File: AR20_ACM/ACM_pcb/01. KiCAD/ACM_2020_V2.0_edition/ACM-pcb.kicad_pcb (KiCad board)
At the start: 2 copper layers, 19.8 x 28 mm, 32 parts, among them IC1 MCP25625T-E_ML, J1 TC2030-MCP-NL, P1 Conn_02x15_Odd_Even, Q1 Q_PMOS_DGS, U1 ATmega328P-AU, U3 NCV890430MW50TXG, Y1 16.0Mhz

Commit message: Circuit protecion fixed
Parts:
- removed D2: 2.4V, Diode_SMD:D_SOD-523
- added D4: D_Schottky_MBR0520LT1G, ACM_2020_V2:D_schotky_MBR0520LT1G, B.Cu at (74.5, 86.9)
- IC1: footprint ACM_2020_Footprintandsymbol:QFN65P600X600X100-29N-D -> ACM_2020_V2:QFN65P600X600X100-29N-D
- Q1: value Q_PMOS_DGS -> Q_PMOS_DMP3099L-13; footprint Package_TO_SOT_SMD:SOT-23 -> ACM_2020_V2:Pmos_DMP3099L-13; moved to F.Cu
- R2: value 100K Ohm -> 10K Ohm; moved to F.Cu
- moved R2 5.84 mm to (79.9, 89.4), turned to 90 degrees
- moved Q1 4.10 mm to (72.4, 88.4), turned to 90 degrees
- moved R1 1.79 mm to (69.1, 81.1), turned to 270 degrees
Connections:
- D1 pad 1: Net-(D1-Pad1) -> +12V_Safe
- F1 pad 1: Net-(D1-Pad1) -> +12V_Safe
- F1 pad 2: +12V -> Net-(D4-Pad1)
- IC1 pad 14: Net-(IC1-Pad14) -> (no net)
- IC1 pad 17: Net-(IC1-Pad17) -> (no net)
- IC1 pad 20: Net-(IC1-Pad20) -> (no net)
- IC1 pad 23: Net-(IC1-Pad23) -> (no net)
- IC1 pad 24: Net-(IC1-Pad24) -> (no net)
- IC1 pad 6: Net-(IC1-Pad6) -> (no net)
- IC1 pad 7: Net-(IC1-Pad7) -> (no net)
- IC1 pad 8: Net-(IC1-Pad8) -> (no net)
- IC1 pad 9: Net-(IC1-Pad9) -> (no net)
- J1 pad 2: +5V -> Net-(J1-Pad2)
- Q1 pad 1: Net-(D2-Pad2) -> +12V_Safe
- Q1 pad 2: +12V_Safe -> +5V
- Q1 pad 3: Net-(D1-Pad1) -> Net-(J1-Pad2)
- R2 pad 1: Net-(D2-Pad2) -> GND
- R2 pad 2: GND -> +12V_Safe
- U3 pad 2: Net-(U3-Pad2) -> (no net)
- U3 pad 6: Net-(U3-Pad6) -> (no net)
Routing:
- net +12V: track 44.4 -> 32.3 mm, vias 1 -> 0
- net Net-(D1-Pad1): track 5.04 -> 0.00 mm
- net +12V_Safe: track 13.3 -> 18.1 mm
- net Net-(D2-Pad2): track 3.50 -> 0.00 mm
- net Net-(D4-Pad1): track 0.00 -> 3.29 mm
- net Net-(J1-Pad2): track 0.00 -> 2.20 mm
- net /Reset: track 45.9 -> 43.7 mm
- net GND: track 47.1 -> 49.2 mm, vias 10 -> 11
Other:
- board text added: "V1.2"
- board text removed: "V1.1"

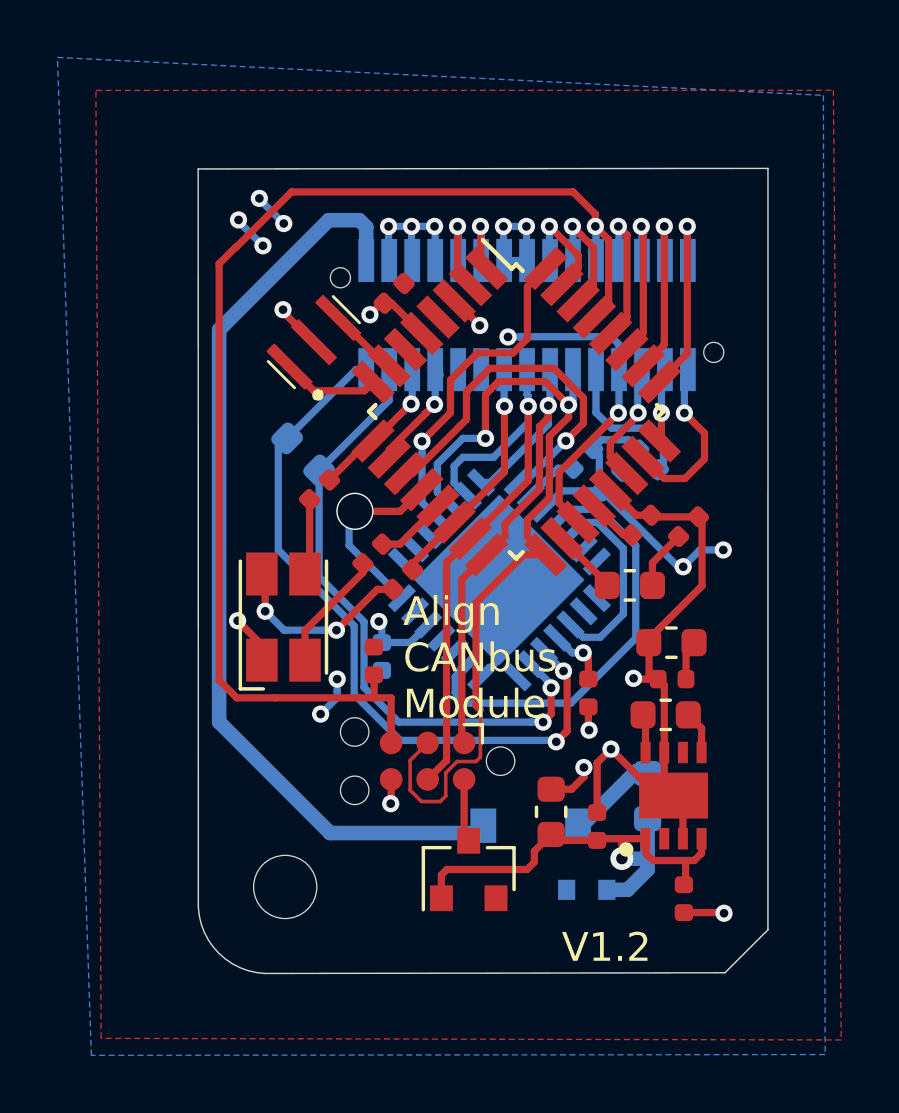
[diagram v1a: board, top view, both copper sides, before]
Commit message: Changed RGB light
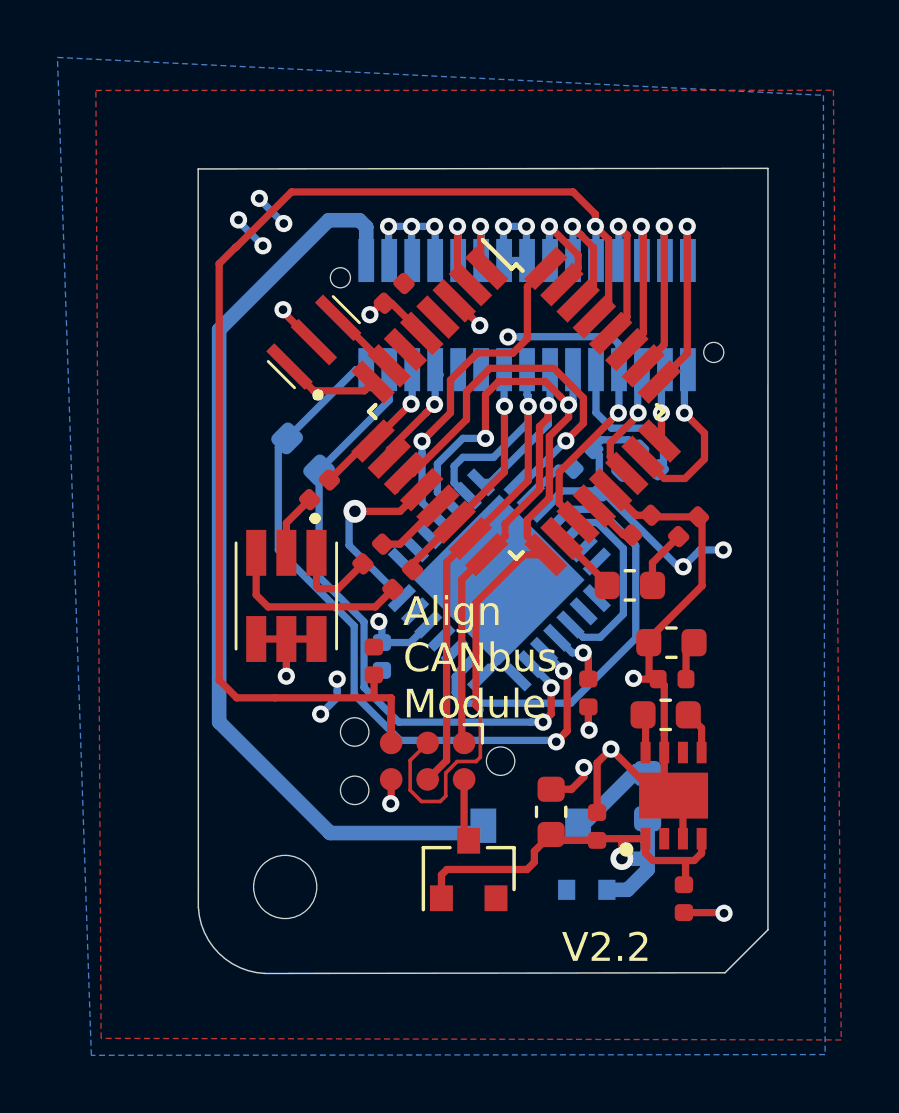
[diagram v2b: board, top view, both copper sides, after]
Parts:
- removed D3: ASMB-MTB0-0A3A2, LED_SMD:LED_Avago_PLCC4_3.2x2.8mm_CW
- added LED1: ASMB-TTF0-0A20B, ASMB-TTF0-0A20B:ASMBTTF00A20B, F.Cu at (66.0, 78.9)
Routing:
- net GND: track 49.2 -> 52.6 mm, vias 11 -> 12
- net +5V: track 32.7 -> 31.0 mm, vias 14 -> 13
- net Net-(LED1-Pad1): track 4.19 -> 3.17 mm
- net Net-(LED1-Pad5): vias 2 -> 0
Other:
- board text added: "V2.2"
- board text removed: "V1.2"

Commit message: NOT COMPLETE V3.0 ACM
This is the beginning of the V3.0 ACM. With added CAN FD transiver and CAN FD controller. 
To fix: 
Chagne CAN FD transciver to a SOCI version 
Place all capacitors in a good location. 
Board cleanup
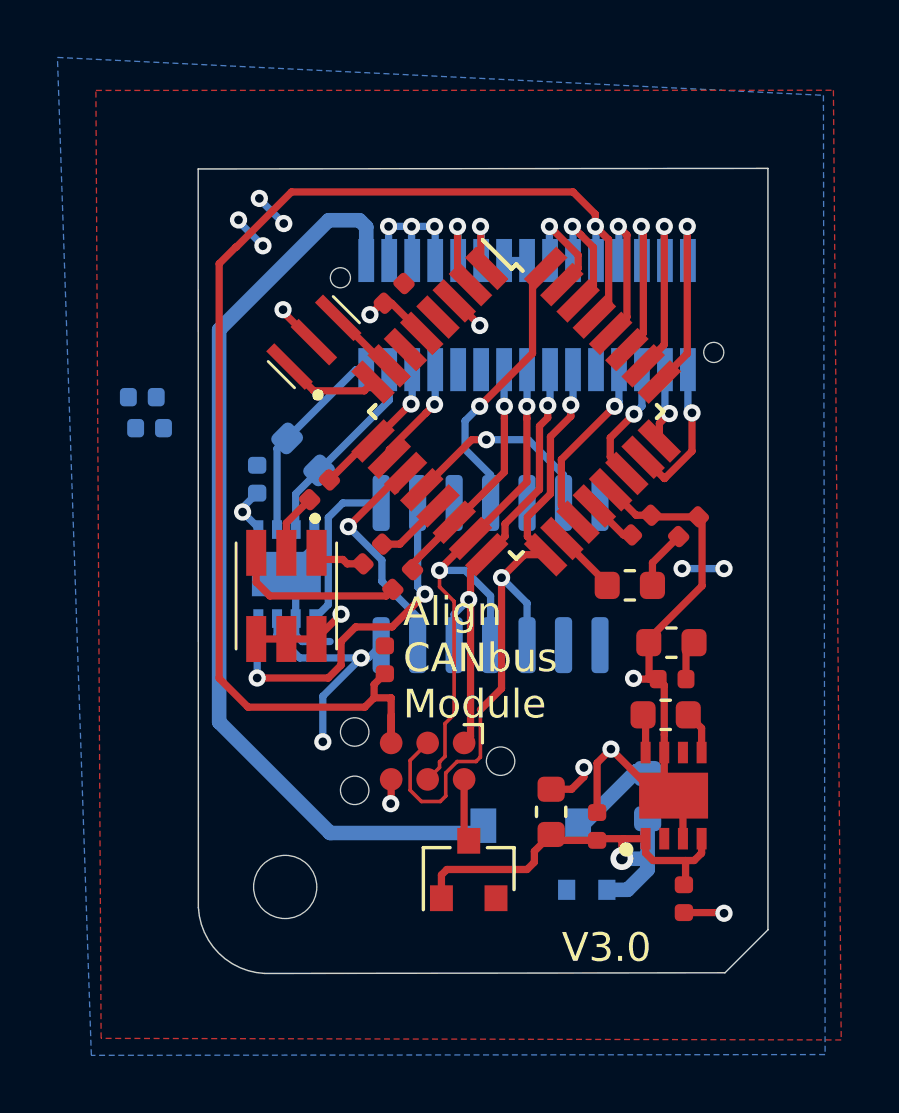
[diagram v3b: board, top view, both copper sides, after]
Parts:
- removed C9: 0.1uF, Capacitor_SMD:C_0402_1005Metric
- removed IC1: MCP25625T-E_ML, ACM_2020_V2:QFN65P600X600X100-29N-D
- removed R6: 10K Ohm, Resistor_SMD:R_0402_1005Metric
- added U2: MCP2542WFDxMF, Package_DFN_QFN:DFN-8-1EP_3x3mm_P0.65mm_EP1.55x2.4mm, B.Cu at (66.0, 78.1)
- added U4: MCP2517FD-xSL, ACM_2020_V2:Can_MCP2517FD_SOIC, B.Cu at (73.2, 78.1)
- R3: value 290 ohm -> R-Device-ACM_Y2020V0.1-rescue
- moved C6 17.4 mm to (61.3, 73.0), turned to 0 degrees
- moved C7 12.4 mm to (65.0, 74.8), turned to 90 degrees
- moved C8 12.3 mm to (61.0, 71.9), turned to 180 degrees
- moved R1 0.38 mm to (69.5, 81.1)
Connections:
- C8 pad 1: +5V -> GND
- C8 pad 2: GND -> +5V
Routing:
- net /U-Pin29: track 25.3 -> 7.06 mm, vias 2 -> 0
- net Net-(IC1-Pad16): track 15.2 -> 0.00 mm
- net /U-Pin27: track 21.9 -> 6.96 mm, vias 2 -> 0
- net /RXCAN: track 0.00 -> 12.9 mm, vias 0 -> 2
- net GND: track 52.6 -> 41.3 mm, vias 12 -> 9
- net Net-(IC1-Pad10): track 7.31 -> 0.00 mm
- net /SCK: track 30.4 -> 24.1 mm
- net +5V: track 31.0 -> 24.8 mm, vias 13 -> 12
- net /TXCAN: track 0.00 -> 5.77 mm
- net /U-Pin7: track 11.5 -> 6.60 mm, vias 2 -> 1
- net /CAN_CS: track 13.1 -> 8.25 mm
- net /MISO: track 18.1 -> 16.0 mm, vias 1 -> 2
- net /CAN_INT: track 11.6 -> 9.70 mm
- net Net-(IC1-Pad2): track 1.86 -> 0.00 mm
- net Net-(LED1-Pad1): track 3.17 -> 1.78 mm
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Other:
- net class Default: clearance 0.0889 -> 0.127
- rule trace_clearance: 0.0889 -> 0.127
- board text added: "Adrian var her"
- board text added: "V3.0"
- board text removed: "V2.2"

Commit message: ACM 3.0 CAN FD implemented and made SOIC
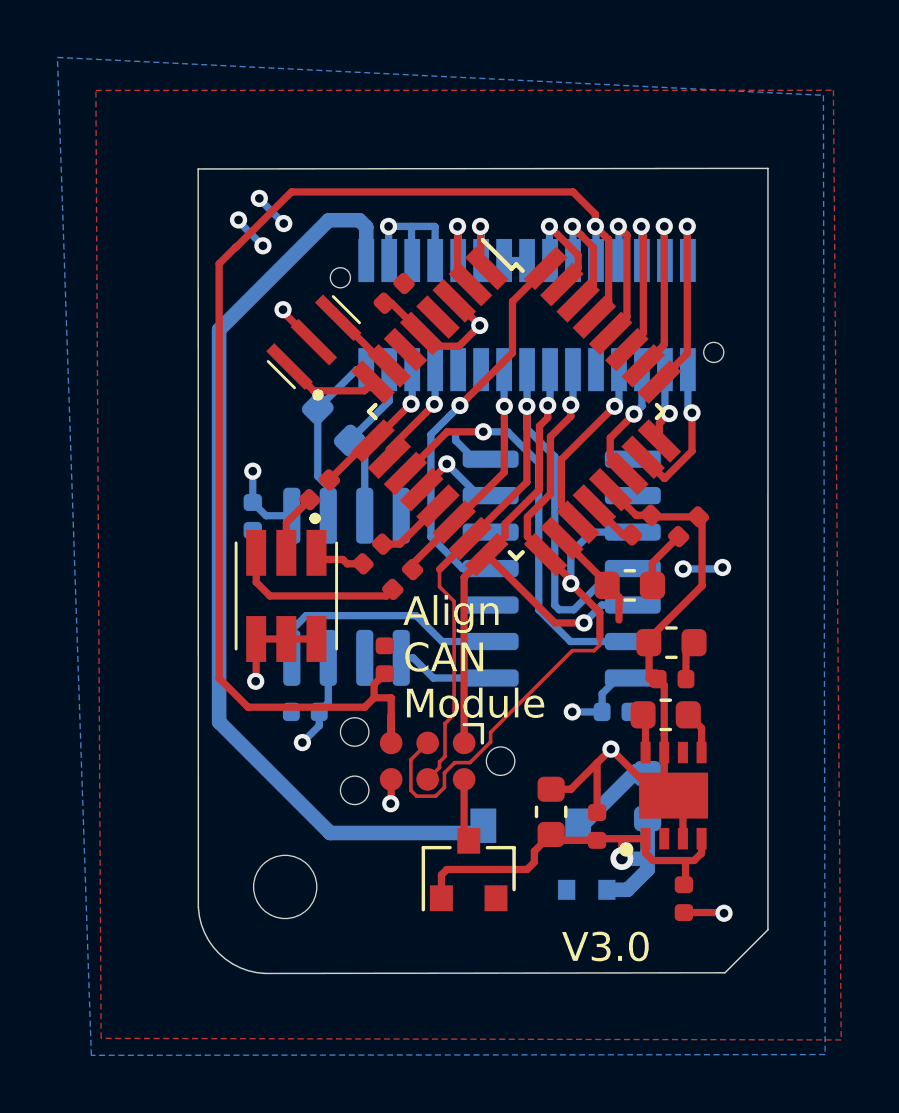
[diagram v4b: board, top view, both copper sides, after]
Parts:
- LED1: footprint ASMB-TTF0-0A20B:ASMBTTF00A20B -> ACM_2020_V2:ASMBTTF00A20B
- U2: value MCP2542WFDxMF -> MCP2542FDxMF; footprint Package_DFN_QFN:DFN-8-1EP_3x3mm_P0.65mm_EP1.55x2.4mm -> ACM_2020_V2:SOIC_MCP2542FD
- moved C6 19.0 mm to (77.5, 82.9)
- moved C8 12.3 mm to (66.7, 82.9), turned to 0 degrees
- moved U4 2.48 mm to (75.6, 77.9), turned to 0 degrees
- moved U2 2.14 mm to (68.1, 78.5)
- moved R7 1.49 mm to (67.7, 72.9)
- moved C7 1.30 mm to (64.9, 76.1), turned to 270 degrees
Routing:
- net /MOSI: track 20.0 -> 26.8 mm, vias 2 -> 1
- net /CAN_CS: track 8.25 -> 14.9 mm
- net /MISO: track 16.0 -> 20.6 mm
- net /RXCAN: track 12.9 -> 8.48 mm, vias 2 -> 0
- net /CLK_MCP: track 7.14 -> 3.24 mm
- net /CAN_INT: track 9.70 -> 13.5 mm
- net /TXCAN: track 5.77 -> 3.40 mm
- net GND: track 41.3 -> 39.1 mm, vias 9 -> 6
- net /SCK: track 24.1 -> 26.0 mm
- net /U-Pin27: track 6.96 -> 5.91 mm
- net /U-Pin29: track 7.06 -> 6.13 mm
- net +5V: track 24.8 -> 25.2 mm, vias 12 -> 10
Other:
- board text added: "Align CAN Module"
- board text removed: "Adrian var her"
- board text removed: "Align CANbus Module"

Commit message: Better connections
Gave groundplane a better route and moved some 5V
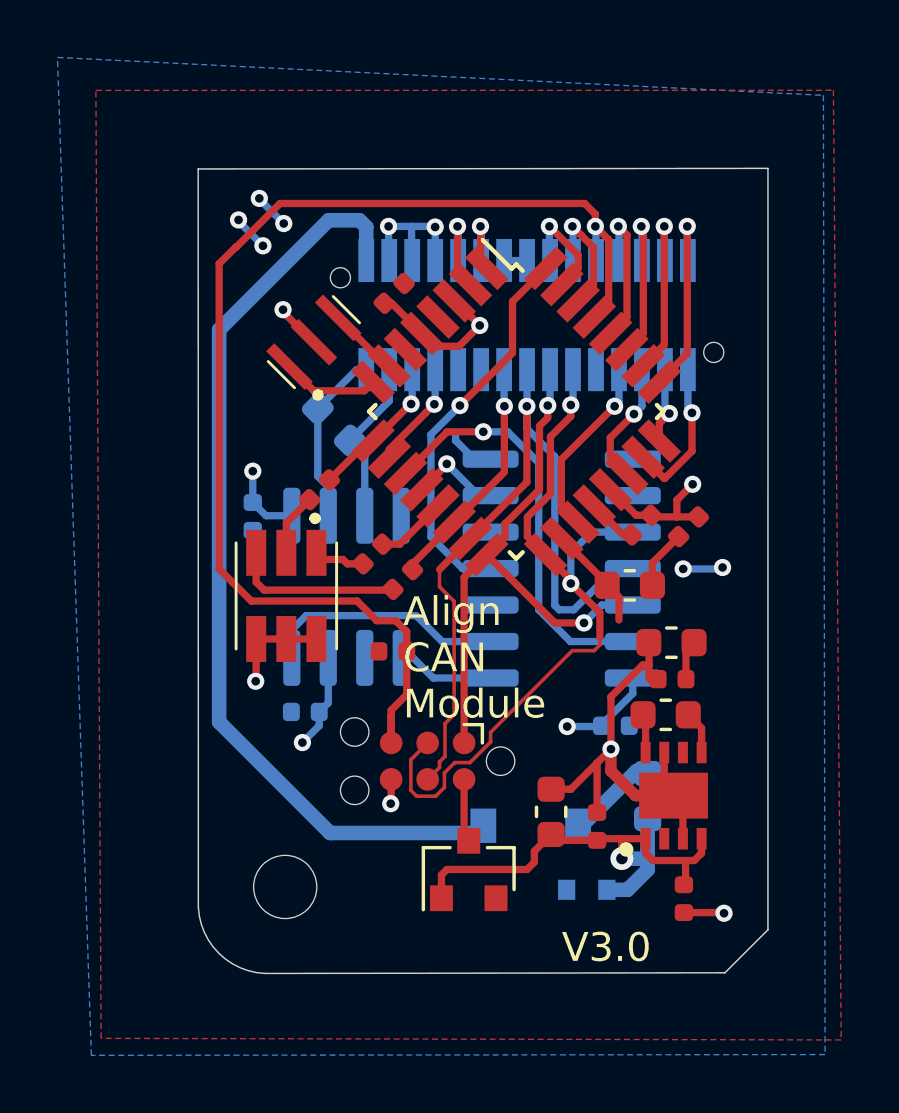
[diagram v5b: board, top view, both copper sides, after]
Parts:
- moved C6 0.48 mm to (77.5, 83.4)
- moved R1 0.40 mm to (69.7, 80.8), turned to 0 degrees
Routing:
- net GND: track 39.1 -> 37.0 mm, vias 6 -> 7
- net /Reset: track 44.1 -> 42.4 mm
- net +5V: track 25.2 -> 25.5 mm, vias 10 -> 11

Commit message: Added Zener diode between 5V and ground
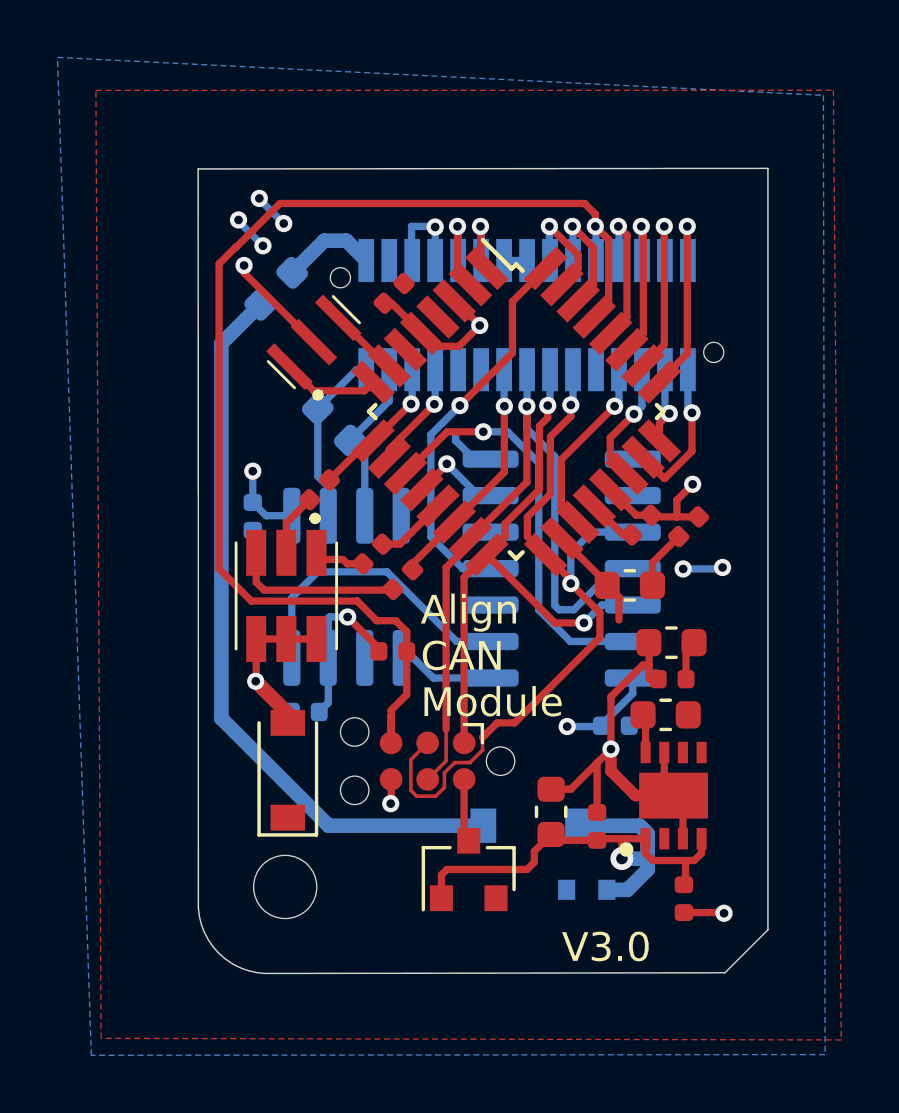
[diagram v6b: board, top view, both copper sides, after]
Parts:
- added D2: D_Zener_KDZVTR5.6B, ACM_2020_V2:D_Zener_KDZV5.6B_SOD-123, F.Cu at (66.1, 84.9)
- moved F1 21.9 mm to (65.7, 68.2), turned to 45 degrees
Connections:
- D4 pad 1: Net-(D4-Pad1) -> +12V_Safe
- D4 pad 2: +12V -> Net-(D4-Pad2)
- F1 pad 1: +12V_Safe -> Net-(D4-Pad2)
- F1 pad 2: Net-(D4-Pad1) -> +12V
- P1 pad 28: +5V -> (no net)
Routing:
- net +12V: track 32.3 -> 3.36 mm
- net Net-(D4-Pad2): track 0.00 -> 25.6 mm
- net GND: track 37.0 -> 41.0 mm
- net Net-(D4-Pad1): track 3.29 -> 0.00 mm
- net +12V_Safe: track 18.1 -> 20.5 mm
- net /RXCAN: track 8.48 -> 10.4 mm
- net +5V: track 25.5 -> 24.4 mm, vias 11 -> 10

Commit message: 20Mhz resonator on CAN Conrtoller
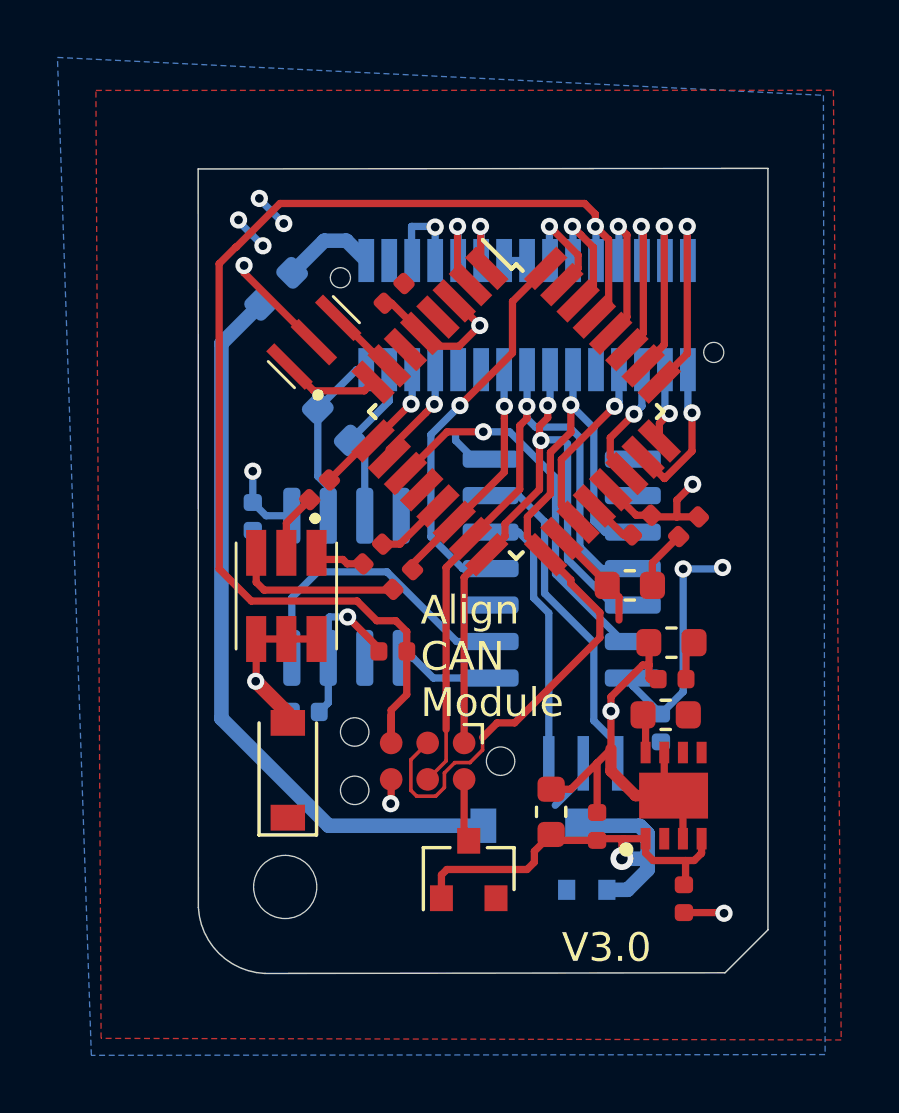
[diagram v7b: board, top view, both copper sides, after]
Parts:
- added Y2: 20.0 Mhz, ACM_2020_V2:Resonator_CSTNE20M0V51Z000R0, B.Cu at (76.4, 84.7)
- R3: value R-Device-ACM_Y2020V0.1-rescue -> 220Ω
- R4: value 200ohm -> 200Ω
- R5: value 190 Ohm -> 190Ω
- R7: value 120 Ohm -> 120Ω
- moved C6 1.59 mm to (79.1, 83.5), turned to 270 degrees
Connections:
- U1 pad 12: /CLK_MCP -> (no net)
- U4 pad 5: (no net) -> Net-(U4-Pad5)
- U4 pad 6: /CLK_MCP -> Net-(U4-Pad6)
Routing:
- net Net-(U4-Pad6): track 0.00 -> 11.7 mm
- net Net-(U4-Pad5): track 0.00 -> 9.46 mm
- net +5V: track 24.4 -> 28.1 mm, vias 10 -> 9
- net /CLK_MCP: track 3.24 -> 0.00 mm, vias 1 -> 0
- net /SCK: track 26.0 -> 28.3 mm, vias 2 -> 1
- net /MOSI: track 26.4 -> 24.2 mm
- net GND: track 41.0 -> 42.9 mm
- net /MISO: track 20.6 -> 22.2 mm
- net /CAN_CS: track 14.9 -> 13.9 mm
